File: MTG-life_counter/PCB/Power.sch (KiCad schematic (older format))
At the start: 6 parts

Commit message: Specify programming resistor and protection diode for charger.
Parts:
- added D1: SMAJ5.0A, Diode_SMD:D_SMA_Handsoldering, symbol Device:D_TVS
- BT1: renamed from BT?; footprint (none) -> Connector_PinHeader_2.54mm:PinHeader_1x02_P2.54mm_Horizontal
- C4, C5: renamed from C?; value C -> 4,7 µF; footprint (none) -> Capacitor_SMD:C_1206_3216Metric_Pad1.42x1.75mm_HandSolder
- R1: renamed from R?; value R -> 3,3 k; footprint (none) -> Resistor_SMD:R_0805_2012Metric_Pad1.20x1.40mm_HandSolder
- gave numbers to parts that had none: 2
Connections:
- net labels added: VUSB
- wire segments 27 -> 34
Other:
- note added: "LiPo 1800 mAh"
- note added: "R1 sets max. charge current of ~~ 303 mA\nR = 1000 V / I"
- moved on the sheet: BT1, C4, C5, J1
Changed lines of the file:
@@
 Comment4 ""
 $EndDescr
-Text Notes 7200 3950 0    50   ~ 0
+Text Notes 7450 3950 0    50   ~ 0
 nominal\nvoltage:\n3.7 V
 $Comp
-L Switch:SW_SPST #SW?
+L Switch:SW_SPST #SW2
 U 1 1 61840AEE
-P 6700 3500
-F 0 "#SW?" H 6700 3735 50  0000 C CNN
-F 1 "SW_SPST" H 6700 3644 50  0000 C CNN
-F 2 "" H 6700 3500 50  0001 C CNN
-F 3 "~" H 6700 3500 50  0001 C CNN
-	1    6700 3500
-	1    0    0    -1
-$EndComp
-$Comp
-L power:VCC #PWR?
+P 6950 3500
+F 0 "#SW2" H 6950 3735 50  0000 C CNN
+F 1 "SW_SPST" H 6950 3644 50  0000 C CNN
+F 2 "" H 6950 3500 50  0001 C CNN
+F 3 "~" H 6950 3500 50  0001 C CNN
+	1    6950 3500
+	1    0    0    -1
+$EndComp
+$Comp
+L power:VCC #PWR012
 U 1 1 61840AF4
-P 7200 3450
-F 0 "#PWR?" H 7200 3300 50  0001 C CNN
-F 1 "VCC" H 7215 3623 50  0000 C CNN
-F 2 "" H 7200 3450 50  0001 C CNN
-F 3 "" H 7200 3450 50  0001 C CNN
-	1    7200 3450
-	1    0    0    -1
-$EndComp
-Wire Wire Line
-	6900 3500 7200 3500
-Wire Wire Line
-	7200 3500 7200 3450
-Wire Wire Line
-	3300 3200 3100 3200
-Wire Wire Line
-	3300 3800 3300 3200
-Wire Wire Line
-	3300 4200 2800 4200
-Connection ~ 3300 4200
-Wire Wire Line
-	3300 4100 3300 4200
-Wire Wire Line
-	5750 4200 6200 4200
-Connection ~ 5750 4200
-Wire Wire Line
-	5750 4000 5750 4200
-Wire Wire Line
-	5750 3700 5750 3500
-$Comp
-L Device:C C?
+P 7450 3450
+F 0 "#PWR012" H 7450 3300 50  0001 C CNN
+F 1 "VCC" H 7465 3623 50  0000 C CNN
+F 2 "" H 7450 3450 50  0001 C CNN
+F 3 "" H 7450 3450 50  0001 C CNN
+	1    7450 3450
+	1    0    0    -1
+$EndComp
+Wire Wire Line
+	7150 3500 7450 3500
+Wire Wire Line
+	7450 3500 7450 3450
+Wire Wire Line
+	2800 2700 2600 2700
+Wire Wire Line
+	2800 3800 2800 2700
+Wire Wire Line
+	2800 4450 2300 4450
+Connection ~ 2800 4450
+Wire Wire Line
+	2800 4100 2800 4450
+Wire Wire Line
+	5750 4450 6450 4450
+Wire Wire Line
+	5750 4100 5750 4450
+Wire Wire Line
+	5750 3800 5750 3500
+$Comp
+L Device:C C5
 U 1 1 61840B05
-P 5750 3850
-F 0 "C?" H 5865 3896 50  0000 L CNN
-F 1 "C" H 5865 3805 50  0000 L CNN
-F 2 "" H 5788 3700 50  0001 C CNN
-F 3 "~" H 5750 3850 50  0001 C CNN
-	1    5750 3850
-	1    0    0    -1
-$EndComp
-$Comp
-L Device:C C?
+P 5750 3950
+F 0 "C5" H 5865 3996 50  0000 L CNN
+F 1 "4,7 µF" H 5865 3905 50  0000 L CNN
+F 2 "Capacitor_SMD:C_1206_3216Metric_Pad1.42x1.75mm_HandSolder" H 5788 3800 50  0001 C CNN
+F 3 "~" H 5750 3950 50  0001 C CNN
+	1    5750 3950
+	1    0    0    -1
+$EndComp
+$Comp
+L Device:C C4
 U 1 1 61840B0B
-P 3300 3950
-F 0 "C?" H 3415 3996 50  0000 L CNN
-F 1 "C" H 3415 3905 50  0000 L CNN
-F 2 "" H 3338 3800 50  0001 C CNN
-F 3 "~" H 3300 3950 50  0001 C CNN
-	1    3300 3950
+P 2800 3950
+F 0 "C4" H 2915 3996 50  0000 L CNN
+F 1 "4,7 µF" H 2915 3905 50  0000 L CNN
+F 2 "Capacitor_SMD:C_1206_3216Metric_Pad1.42x1.75mm_HandSolder" H 2838 3800 50  0001 C CNN
+F 3 "~" H 2800 3950 50  0001 C CNN
+	1    2800 3950
 	1    0    0    -1
 $EndComp
@@
 CHARGE_LED
 Wire Wire Line
-	6200 3500 6500 3500
-Wire Wire Line
-	5750 3500 6200 3500
-Connection ~ 6200 3500
-Wire Wire Line
-	6200 3500 6200 3450
-$Comp
-L power:+BATT #PWR?
+	6450 3500 6750 3500
+Wire Wire Line
+	5750 3500 6450 3500
+Connection ~ 6450 3500
+Wire Wire Line
+	6450 3500 6450 3450
+$Comp
+L power:+BATT #PWR09
 U 1 1 61840B17
-P 6200 3450
-F 0 "#PWR?" H 6200 3300 50  0001 C CNN
-F 1 "+BATT" H 6215 3623 50  0000 C CNN
-F 2 "" H 6200 3450 50  0001 C CNN
-F 3 "" H 6200 3450 50  0001 C CNN
-	1    6200 3450
+P 6450 3450
+F 0 "#PWR09" H 6450 3300 50  0001 C CNN
+F 1 "+BATT" H 6465 3623 50  0000 C CNN
+F 2 "" H 6450 3450 50  0001 C CNN
+F 3 "" H 6450 3450 50  0001 C CNN
+	1    6450 3450
 	1    0    0    -1
 $EndComp
@@
 	3850 3800 3850 3700
 Wire Wire Line
-	3850 4200 3300 4200
-Connection ~ 3850 4200
-Wire Wire Line
-	3850 4100 3850 4200
-$Comp
-L Device:R R?
+	3850 4450 3300 4450
+Wire Wire Line
+	3850 4100 3850 4450
+$Comp
+L Device:R R1
 U 1 1 61840B22
 P 3850 3950
-F 0 "R?" H 3920 3996 50  0000 L CNN
-F 1 "R" H 3920 3905 50  0000 L CNN
-F 2 "" V 3780 3950 50  0001 C CNN
+F 0 "R1" H 3920 3996 50  0000 L CNN
+F 1 "3,3 k" H 3920 3905 50  0000 L CNN
+F 2 "Resistor_SMD:R_0805_2012Metric_Pad1.20x1.40mm_HandSolder" V 3780 3950 50  0001 C CNN
 F 3 "~" H 3850 3950 50  0001 C CNN
 	1    3850 3950
@@
 $EndComp
 Wire Wire Line
-	6200 4200 6200 4000
-Wire Wire Line
-	2800 4200 2800 4250
-Connection ~ 2800 4200
-Wire Wire Line
-	2800 3800 2800 4200
-Wire Wire Line
-	6200 3500 6200 3700
-Connection ~ 5750 3500
+	6450 4450 6450 4100
+Wire Wire Line
+	2300 4450 2300 4500
+Connection ~ 2300 4450
+Wire Wire Line
+	2300 3300 2300 4450
+Wire Wire Line
+	6450 3500 6450 3800
 Wire Wire Line
 	4850 3500 5750 3500
-NoConn ~ 3100 3600
-NoConn ~ 3100 3500
-NoConn ~ 3100 3400
-Wire Wire Line
-	4450 4200 5750 4200
-Wire Wire Line
-	4450 4200 3850 4200
-Connection ~ 4450 4200
-Wire Wire Line
-	4450 3900 4450 4200
-Connection ~ 3300 3200
-Wire Wire Line
-	4450 3200 3300 3200
-Wire Wire Line
-	4450 3300 4450 3200
-$Comp
-L Battery_Management:MCP73831-2-OT U?
+NoConn ~ 2600 3100
+NoConn ~ 2600 3000
+NoConn ~ 2600 2900
+Wire Wire Line
+	4450 4450 5750 4450
+Wire Wire Line
+	4450 4450 3850 4450
+Connection ~ 4450 4450
+Wire Wire Line
+	4450 3900 4450 4450
+Connection ~ 2800 2700
+Wire Wire Line
+	4450 2700 3300 2700
+Wire Wire Line
+	4450 3300 4450 2700
+$Comp
+L Battery_Management:MCP73831-2-OT U1
 U 1 1 61840B39
 P 4450 3600
-F 0 "U?" H 4550 4000 50  0000 L CNN
+F 0 "U1" H 4550 4000 50  0000 L CNN
 F 1 "MCP73831-2-OT" H 4550 3900 50  0000 L CNN
 F 2 "Package_TO_SOT_SMD:SOT-23-5" H 4500 3350 50  0001 L CIN
@@
 $EndComp
 $Comp
-L Connector:USB_B_Mini J?
+L Connector:USB_B_Mini J1
 U 1 1 61840B3F
-P 2800 3400
-F 0 "J?" H 2857 3867 50  0000 C CNN
-F 1 "USB_B_Mini" H 2857 3776 50  0000 C CNN
-F 2 "mibe:USB_Mini-B_Reichelt_BWM" H 2950 3350 50  0001 C CNN
-F 3 "~" H 2950 3350 50  0001 C CNN
-	1    2800 3400
-	1    0    0    -1
-$EndComp
-$Comp
-L power:GND #PWR?
+P 2300 2900
+F 0 "J1" H 2357 3367 50  0000 C CNN
+F 1 "USB_B_Mini" H 2357 3276 50  0000 C CNN
+F 2 "mibe:USB_Mini-B_Reichelt_BWM" H 2450 2850 50  0001 C CNN
+F 3 "~" H 2450 2850 50  0001 C CNN
+	1    2300 2900
+	1    0    0    -1
+$EndComp
+$Comp
+L power:GND #PWR01
 U 1 1 61840B45
-P 2800 4250
-F 0 "#PWR?" H 2800 4000 50  0001 C CNN
-F 1 "GND" H 2805 4077 50  0000 C CNN
-F 2 "" H 2800 4250 50  0001 C CNN
-F 3 "" H 2800 4250 50  0001 C CNN
-	1    2800 4250
-	1    0    0    -1
-$EndComp
-$Comp
-L Device:Battery_Cell BT?
+P 2300 4500
+F 0 "#PWR01" H 2300 4250 50  0001 C CNN
+F 1 "GND" H 2305 4327 50  0000 C CNN
+F 2 "" H 2300 4500 50  0001 C CNN
+F 3 "" H 2300 4500 50  0001 C CNN
+	1    2300 4500
+	1    0    0    -1
+$EndComp
+$Comp
+L Device:Battery_Cell BT1
 U 1 1 61840B4B
-P 6200 3900
-F 0 "BT?" H 6318 3996 50  0000 L CNN
-F 1 "Battery_Cell" H 6318 3905 50  0000 L CNN
-F 2 "" V 6200 3960 50  0001 C CNN
-F 3 "~" V 6200 3960 50  0001 C CNN
-	1    6200 3900
-	1    0    0    -1
-$EndComp
+P 6450 4000
+F 0 "BT1" H 6568 4096 50  0000 L CNN
+F 1 "Battery_Cell" H 6568 4005 50  0000 L CNN
+F 2 "Connector_PinHeader_2.54mm:PinHeader_1x02_P2.54mm_Horizontal" V 6450 4060 50  0001 C CNN
+F 3 "~" V 6450 4060 50  0001 C CNN
+	1    6450 4000
+	1    0    0    -1
+$EndComp
+Text Notes 7450 4150 0    50   ~ 0
+LiPo 1800 mAh
+Text Notes 3850 4750 0    50   ~ 0
+R1 sets max. charge current of ~~ 303 mA\nR = 1000 V / I
+$Comp
+L Device:D_TVS D1
+U 1 1 6189FBE0
+P 3300 3950
+F 0 "D1" V 3254 4030 50  0000 L CNN
+F 1 "SMAJ5.0A" V 3345 4030 50  0000 L CNN
+F 2 "Diode_SMD:D_SMA_Handsoldering" H 3300 3950 50  0001 C CNN
+F 3 "~" H 3300 3950 50  0001 C CNN
+	1    3300 3950
+	0    1    1    0
+$EndComp
+Connection ~ 3850 4450
+Wire Wire Line
+	3300 4100 3300 4450
+Connection ~ 3300 4450
+Wire Wire Line
+	3300 4450 2800 4450
+Wire Wire Line
+	3300 3800 3300 2700
+Connection ~ 3300 2700
+Connection ~ 5750 4450
+Connection ~ 5750 3500
+$Comp
+L power:PWR_FLAG #FLG?
+U 1 1 618A58D2
+P 3050 2650
+F 0 "#FLG?" H 3050 2725 50  0001 C CNN
+F 1 "PWR_FLAG" H 3050 2823 50  0000 C CNN
+F 2 "" H 3050 2650 50  0001 C CNN
+F 3 "~" H 3050 2650 50  0001 C CNN
+	1    3050 2650
+	1    0    0    -1
+$EndComp
+Wire Wire Line
+	3300 2700 3050 2700
+Wire Wire Line
+	3050 2700 2800 2700
+Connection ~ 3050 2700
+Wire Wire Line
+	3050 2650 3050 2700
+Text HLabel 4700 2700 2    50   Output ~ 0
+VUSB
+Wire Wire Line
+	4700 2700 4450 2700
+Connection ~ 4450 2700
 $EndSCHEMATC

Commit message: Add a voltage monitor to be used to reset the microcontroller.
This is used as sort of a undervoltage lockout protection to protect the battery. The threshold voltage of the used IC is 3.08 V, which is near the minimum discharge voltage of a LiPo battery of 3 V.
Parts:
- added R10: 680 Ω, Resistor_SMD:R_0805_2012Metric_Pad1.20x1.40mm_HandSolder, symbol Device:R
- added U5: SGM809, Package_TO_SOT_SMD:SOT-23W_Handsoldering, symbol mibe:SGM809
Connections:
- net labels added: CHARGER_STAT, ~BATT_LOW
- net labels removed: CHARGE_LED
- wire segments 34 -> 40
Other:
- note added: ""UVLO""
- note added: "LiPo 1800 mAh\nnominal voltage: 3.7 V"
- note removed: "LiPo 1800 mAh"
- note removed: "nominal\nvoltage:\n3.7 V"
- moved on the sheet: BT1, C4, C5, D1, R1, U1

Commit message: Power schematic is pretty much done.
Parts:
- R1: value 3,3 k -> 3,3 kΩ
- U5: value SGM809 -> SGM809-T
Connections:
- net labels removed: SW_SPST, VCC
- wire segments 40 -> 42
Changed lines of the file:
@@
 Comment4 ""
 $EndDescr
-$Comp
-L Switch:SW_SPST #SW2
-U 1 1 61840AEE
-P 8550 3100
-F 0 "#SW2" H 8550 3335 50  0000 C CNN
-F 1 "SW_SPST" H 8550 3244 50  0000 C CNN
-F 2 "" H 8550 3100 50  0001 C CNN
-F 3 "~" H 8550 3100 50  0001 C CNN
-	1    8550 3100
-	1    0    0    -1
-$EndComp
-$Comp
-L power:VCC #PWR012
-U 1 1 61840AF4
-P 9050 3050
-F 0 "#PWR012" H 9050 2900 50  0001 C CNN
-F 1 "VCC" H 9065 3223 50  0000 C CNN
-F 2 "" H 9050 3050 50  0001 C CNN
-F 3 "" H 9050 3050 50  0001 C CNN
-	1    9050 3050
-	1    0    0    -1
-$EndComp
-Wire Wire Line
-	8750 3100 9050 3100
-Wire Wire Line
-	9050 3100 9050 3050
 Wire Wire Line
 	2800 4050 2800 2700
@@
 	5750 3100 6450 3100
 Connection ~ 6450 3100
-Wire Wire Line
-	6450 3100 6450 3050
 $Comp
 L power:+BATT #PWR09
 U 1 1 61840B17
-P 6450 3050
-F 0 "#PWR09" H 6450 2900 50  0001 C CNN
-F 1 "+BATT" H 6465 3223 50  0000 C CNN
-F 2 "" H 6450 3050 50  0001 C CNN
-F 3 "" H 6450 3050 50  0001 C CNN
-	1    6450 3050
+P 8350 3050
+F 0 "#PWR09" H 8350 2900 50  0001 C CNN
+F 1 "+BATT" H 8365 3223 50  0000 C CNN
+F 2 "" H 8350 3050 50  0001 C CNN
+F 3 "" H 8350 3050 50  0001 C CNN
+	1    8350 3050
 	1    0    0    -1
 $EndComp
@@
 P 3850 4200
 F 0 "R1" H 3920 4246 50  0000 L CNN
-F 1 "3,3 k" H 3920 4155 50  0000 L CNN
+F 1 "3,3 kΩ" H 3920 4155 50  0000 L CNN
 F 2 "Resistor_SMD:R_0805_2012Metric_Pad1.20x1.40mm_HandSolder" V 3780 4200 50  0001 C CNN
 F 3 "~" H 3850 4200 50  0001 C CNN
@@
 Connection ~ 2300 4900
 Wire Wire Line
-	2300 3300 2300 4900
+	2300 3300 2300 3400
 Wire Wire Line
 	6450 3100 6450 4050
@@
 Connection ~ 5750 4900
 Connection ~ 5750 3100
-$Comp
-L power:PWR_FLAG #FLG0101
-U 1 1 618A58D2
-P 3050 2650
-F 0 "#FLG0101" H 3050 2725 50  0001 C CNN
-F 1 "PWR_FLAG" H 3050 2823 50  0000 C CNN
-F 2 "" H 3050 2650 50  0001 C CNN
-F 3 "~" H 3050 2650 50  0001 C CNN
-	1    3050 2650
-	1    0    0    -1
-$EndComp
-Connection ~ 3050 2700
-Wire Wire Line
-	3050 2650 3050 2700
 Text HLabel 4700 2700 2    50   Output ~ 0
 VUSB
@@
 U 1 1 618B80FF
 P 7700 4200
-F 0 "U5" H 7470 4246 50  0000 R CNN
-F 1 "SGM809" H 7470 4155 50  0000 R CNN
+F 0 "U5" H 7700 3800 50  0000 L CNN
+F 1 "SGM809-T" H 7700 3700 50  0000 L CNN
 F 2 "Package_TO_SOT_SMD:SOT-23W_Handsoldering" H 7300 4350 50  0001 C CNN
 F 3 "http://www.sg-micro.com/uploads/soft/20190626/1561528457.pdf" H 7400 4450 50  0001 C CNN
@@
 CHARGER_STAT
 Wire Wire Line
-	4850 3300 4950 3300
-Wire Wire Line
 	2600 2700 2800 2700
-Wire Wire Line
-	3050 2700 3300 2700
 Wire Wire Line
 	6450 3100 7600 3100
 Connection ~ 2800 2700
-Wire Wire Line
-	2800 2700 3050 2700
 Connection ~ 3300 2700
 Wire Wire Line
@@
 Wire Wire Line
 	7600 3300 7600 3100
-Connection ~ 7600 3100
-Wire Wire Line
-	7600 3100 8350 3100
-Wire Wire Line
-	7600 3600 7600 3800
 Text Notes 7600 5100 0    50   ~ 0
 "UVLO"
+Connection ~ 7600 3100
+$Comp
+L power:PWR_FLAG #FLG0102
+U 1 1 618C90E1
+P 7500 3700
+F 0 "#FLG0102" H 7500 3775 50  0001 C CNN
+F 1 "PWR_FLAG" H 7500 3873 50  0000 C CNN
+F 2 "" H 7500 3700 50  0001 C CNN
+F 3 "~" H 7500 3700 50  0001 C CNN
+	1    7500 3700
+	0    -1   -1   0
+$EndComp
+Connection ~ 2600 2700
+Wire Wire Line
+	2600 2700 2450 2700
+Wire Wire Line
+	4850 3300 4950 3300
+Wire Wire Line
+	2200 3300 2200 3400
+Wire Wire Line
+	2200 3400 2300 3400
+Connection ~ 2300 3400
+Wire Wire Line
+	2300 3400 2300 4900
+Wire Wire Line
+	7600 3600 7600 3700
+Wire Wire Line
+	2800 2700 3300 2700
+Wire Wire Line
+	7600 3100 8350 3100
+Wire Wire Line
+	7500 3700 7600 3700
+Connection ~ 7600 3700
+Wire Wire Line
+	7600 3700 7600 3800
+Wire Wire Line
+	8350 3100 8350 3050
 $EndSCHEMATC

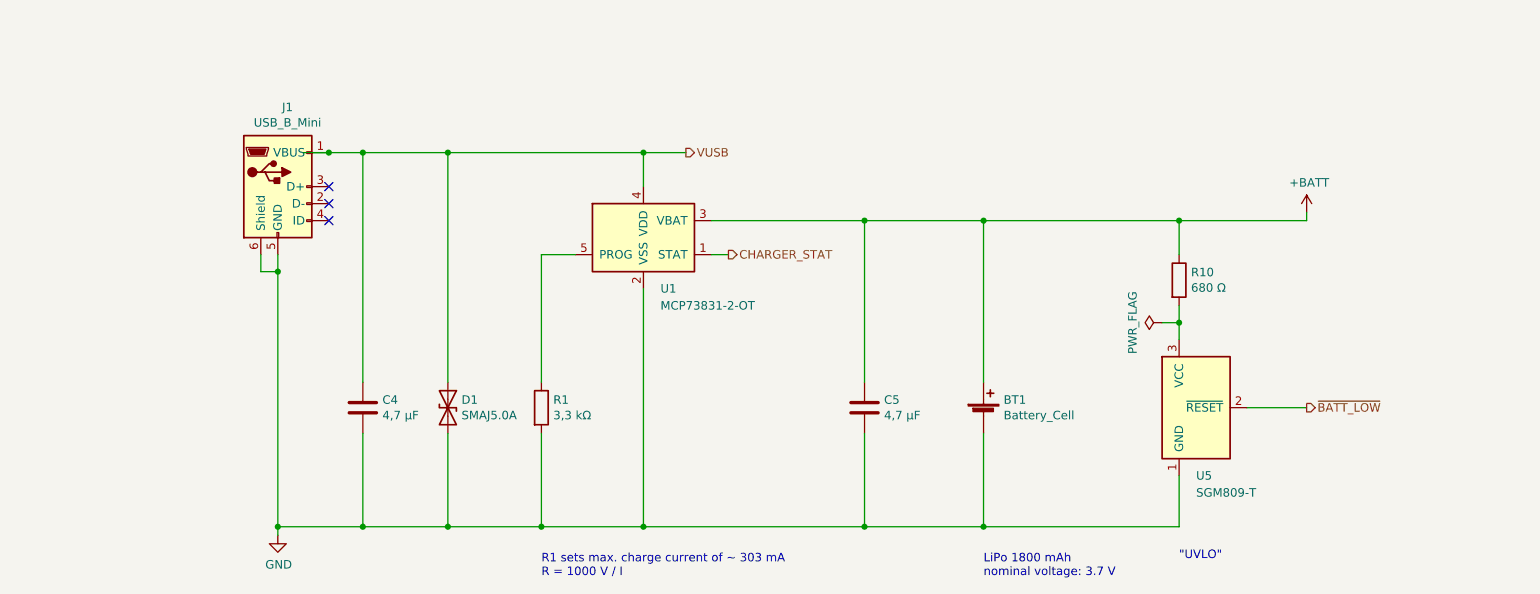
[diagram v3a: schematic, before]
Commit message: Change the USB B mini charging connector to USB C (see #6). Still needs to be placed and routed.
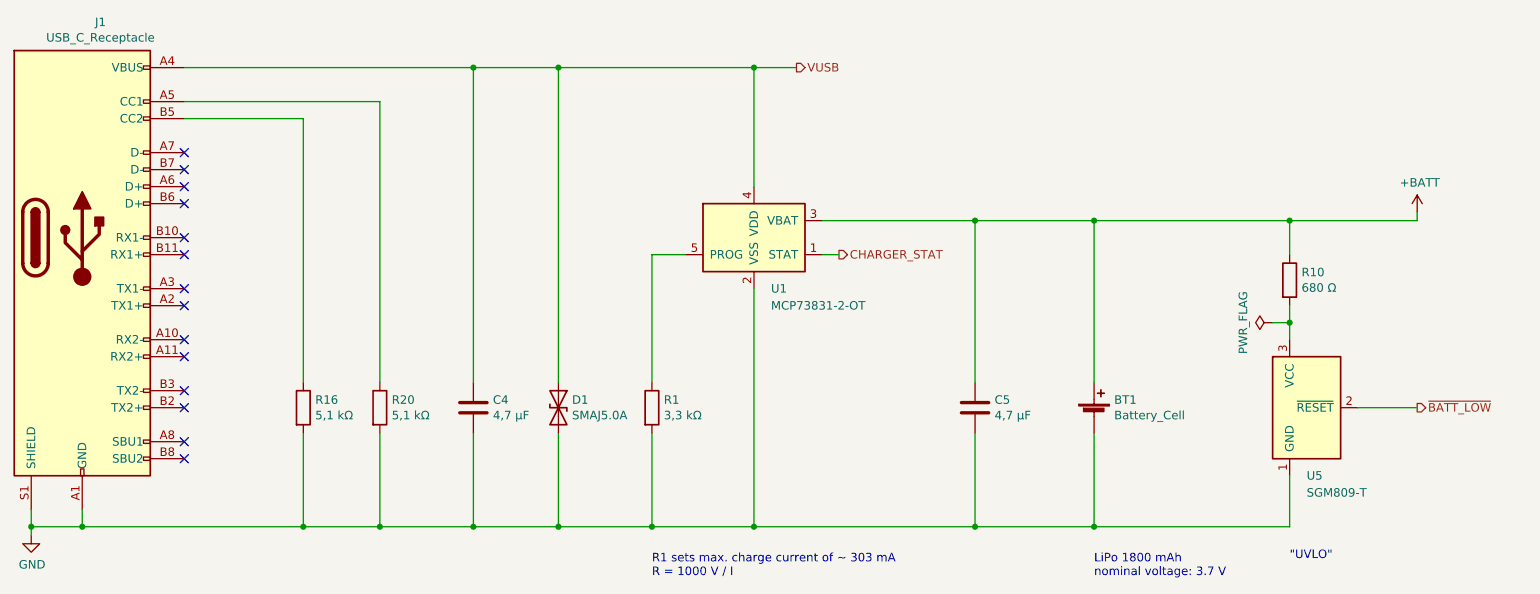
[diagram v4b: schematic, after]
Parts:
- removed J1: USB_B_Mini, mibe:USB_Mini-B_Reichelt_BWM, symbol Connector:USB_B_Mini
- added J1: USB_C_Receptacle, mibe:USB_C_Receptacle_Bellwether_80211-x92, symbol Connector:USB_C_Receptacle
- added R16, R20: 5,1 kΩ, Resistor_SMD:R_0805_2012Metric_Pad1.20x1.40mm_HandSolder, symbol Device:R
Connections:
- wire segments 42 -> 48
- no-connect marks 3 -> 14
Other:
- moved on the sheet: BT1, C4, C5, D1, R1, R10, U1, U5

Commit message: USB C connector placed and routed.
This fixes #6.
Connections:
- net CC1: now reaches J1.A5 (CC1), R20.1
- net CC2: now reaches J1.B5 (CC2), R16.1
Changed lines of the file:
@@
 NoConn ~ 1750 2800
 NoConn ~ 1750 2700
+Text Label 2050 2400 0    50   ~ 0
+CC1
+Text Label 2050 2500 0    50   ~ 0
+CC2
 $EndSCHEMATC

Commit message: Add an on/off switch. This fixes #7.
Also fix ERC errors, rename nets to indicate the signals logic level, move some components a bit and update BOM & netlist.

This is rev. 22/2 of the board.
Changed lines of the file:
@@
 Connection ~ 3950 2200
 Wire Wire Line
-	3950 2200 5100 2200
+	3950 2200 4550 2200
 $Comp
 L Device:R R10
@@
 Text Label 2050 2500 0    50   ~ 0
 CC2
+$Comp
+L power:PWR_FLAG #FLG0103
+U 1 1 639C798F
+P 4550 2250
+F 0 "#FLG0103" H 4550 2325 50  0001 C CNN
+F 1 "PWR_FLAG" H 4550 2423 50  0000 C CNN
+F 2 "" H 4550 2250 50  0001 C CNN
+F 3 "~" H 4550 2250 50  0001 C CNN
+	1    4550 2250
+	-1   0    0    1
+$EndComp
+Wire Wire Line
+	4550 2250 4550 2200
+Connection ~ 4550 2200
+Wire Wire Line
+	4550 2200 5100 2200
 $EndSCHEMATC
